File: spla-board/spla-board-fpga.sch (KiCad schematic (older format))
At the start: 4 parts, among them J2 J_JTAG, U1 LFE5U-45F-BG256

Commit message: schematic: Swap 0402 footprints for 0603.
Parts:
- R13, R14: footprint Resistor_SMD:R_0402_1005Metric -> Resistor_SMD:R_0603_1608Metric
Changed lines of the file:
@@
 F 0 "R13" H 3459 9796 50  0000 L CNN
 F 1 "4.7k" H 3459 9705 50  0000 L CNN
-F 2 "Resistor_SMD:R_0402_1005Metric" H 3400 9750 50  0001 C CNN
+F 2 "Resistor_SMD:R_0603_1608Metric" H 3400 9750 50  0001 C CNN
 F 3 "~" H 3400 9750 50  0001 C CNN
 	1    3400 9750
@@
 F 0 "R14" H 3459 10496 50  0000 L CNN
 F 1 "4.7k" H 3459 10405 50  0000 L CNN
-F 2 "Resistor_SMD:R_0402_1005Metric" H 3400 10450 50  0001 C CNN
+F 2 "Resistor_SMD:R_0603_1608Metric" H 3400 10450 50  0001 C CNN
 F 3 "~" H 3400 10450 50  0001 C CNN
 	1    3400 10450

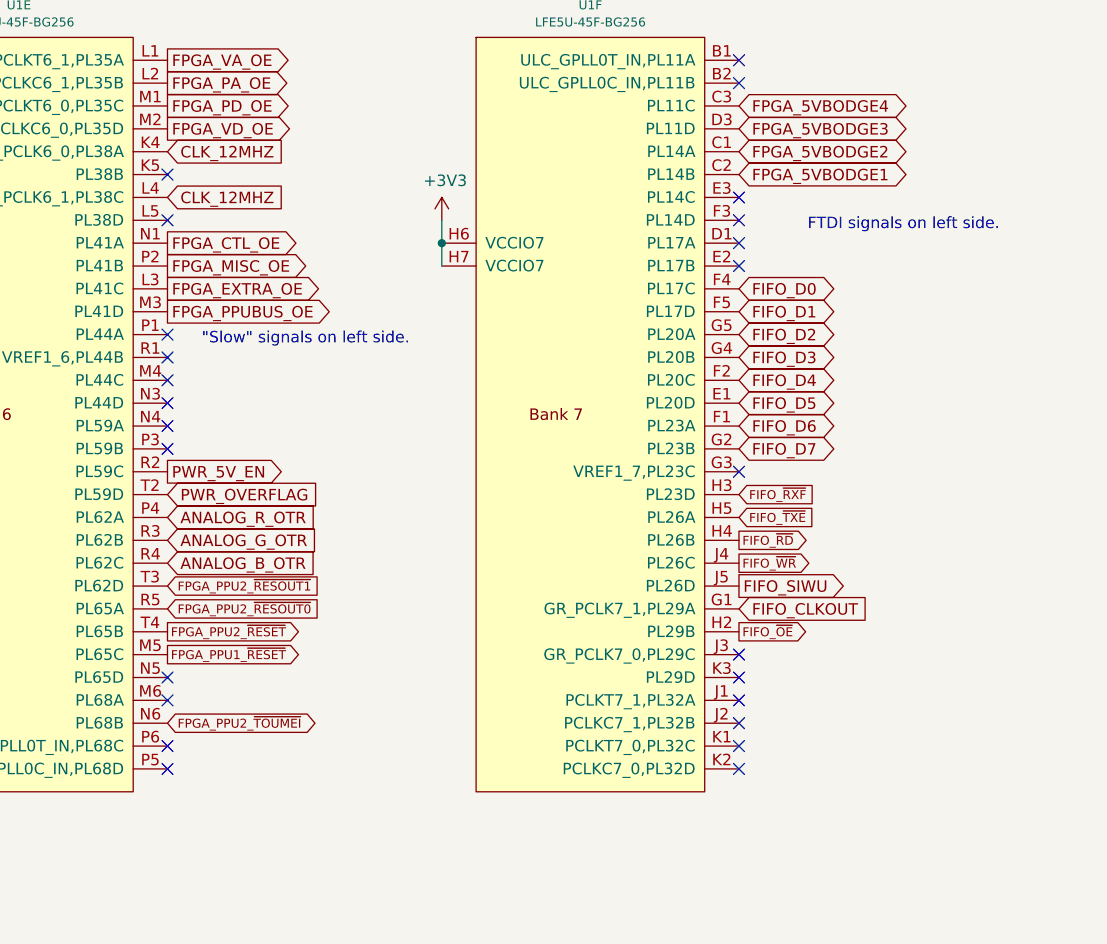
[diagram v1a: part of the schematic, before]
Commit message: schematic: Hook up TST pins to FPGA (via level shifters).
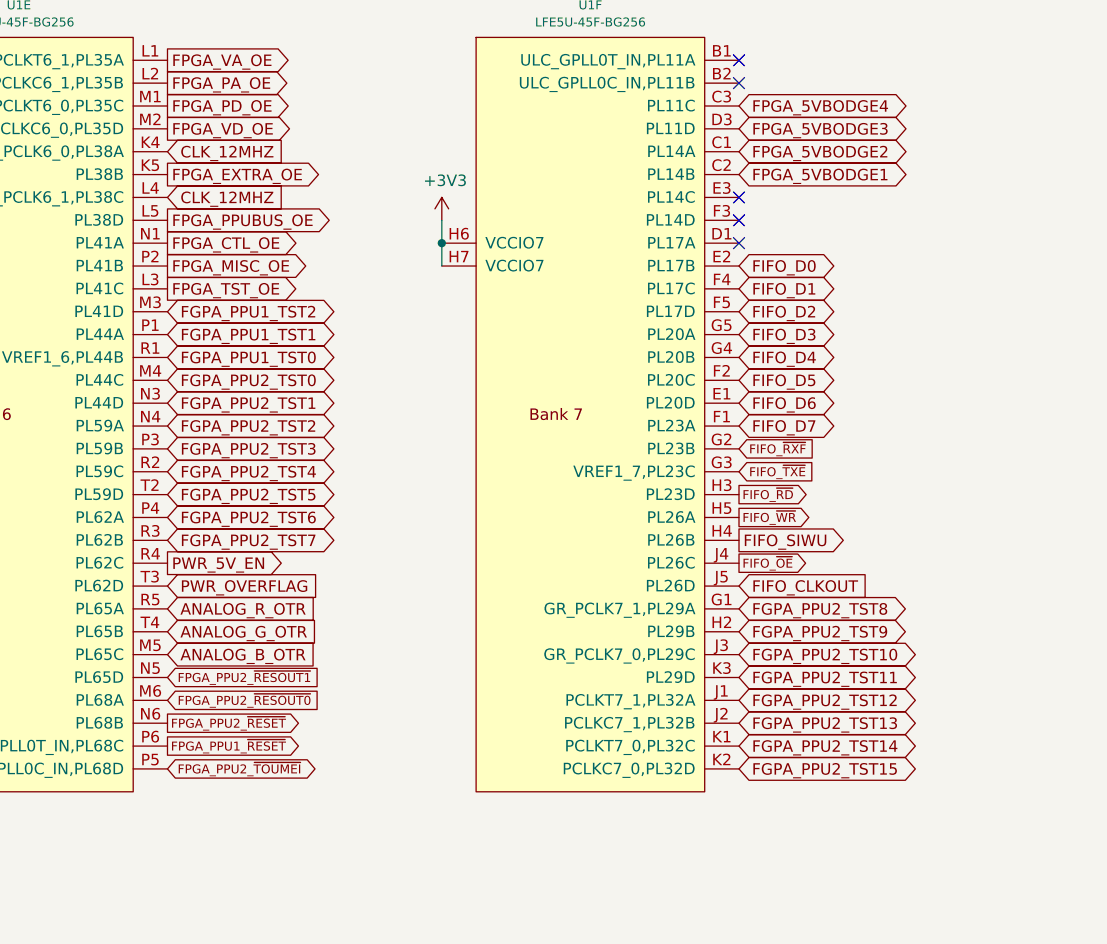
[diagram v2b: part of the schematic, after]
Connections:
- net ANALOG_B_OTR: now also U1.M5 (PL65C); no longer U1.R4 (PL62C)
- net ANALOG_G_OTR: now also U1.T4 (PL65B); no longer U1.R3 (PL62B)
- net ANALOG_R_OTR: now also U1.R5 (PL65A); no longer U1.P4 (PL62A)
- net FIFO_CLKOUT: now also U1.J5 (PL26D); no longer U1.G1 (GR_PCLK7_1,PL29A)
- net FIFO_D0: now also U1.E2 (PL17B); no longer U1.F4 (PL17C)
- net FIFO_D1: now also U1.F4 (PL17C); no longer U1.F5 (PL17D)
- net FIFO_D2: now also U1.F5 (PL17D); no longer U1.G5 (PL20A)
- net FIFO_D3: now also U1.G5 (PL20A); no longer U1.G4 (PL20B)
- net FIFO_D4: now also U1.G4 (PL20B); no longer U1.F2 (PL20C)
- net FIFO_D5: now also U1.F2 (PL20C); no longer U1.E1 (PL20D)
- net FIFO_D6: now also U1.E1 (PL20D); no longer U1.F1 (PL23A)
- net FIFO_D7: now also U1.F1 (PL23A); no longer U1.G2 (PL23B)
- net FIFO_SIWU: now also U1.H4 (PL26B); no longer U1.J5 (PL26D)
- net FIFO_~OE~: now also U1.J4 (PL26C); no longer U1.H2 (PL29B)
- net FIFO_~RD~: now also U1.H3 (PL23D); no longer U1.H4 (PL26B)
- net FIFO_~RXF~: now also U1.G2 (PL23B); no longer U1.H3 (PL23D)
- net FIFO_~TXE~: now also U1.G3 (VREF1_7,PL23C); no longer U1.H5 (PL26A)
- net FIFO_~WR~: now also U1.H5 (PL26A); no longer U1.J4 (PL26C)
- net FPGA_EXTRA_OE: now also U1.K5 (PL38B); no longer U1.L3 (PL41C)
- net FPGA_PPU1_~RESET~: now also U1.P6 (LLC_GPLL0T_IN,PL68C); no longer U1.M5 (PL65C)
- net FPGA_PPU2_~RESET~: now also U1.N6 (PL68B); no longer U1.T4 (PL65B)
- net FPGA_PPU2_~RESOUT0~: now also U1.M6 (PL68A); no longer U1.R5 (PL65A)
- net FPGA_PPU2_~RESOUT1~: now also U1.N5 (PL65D); no longer U1.T3 (PL62D)
- net FPGA_PPU2_~TOUMEI~: now also U1.P5 (LLC_GPLL0C_IN,PL68D); no longer U1.N6 (PL68B)
- net FPGA_PPUBUS_OE: now also U1.L5 (PL38D); no longer U1.M3 (PL41D)
- net PWR_5V_EN: now also U1.R4 (PL62C); no longer U1.R2 (PL59C)
- net PWR_OVERFLAG: now also U1.T3 (PL62D); no longer U1.T2 (PL59D)
- net FGPA_PPU2_TST0: now reaches U1.M4 (PL44C)
- net FGPA_PPU2_TST1: now reaches U1.N3 (PL44D)
- net FGPA_PPU2_TST2: now reaches U1.N4 (PL59A)
- net FGPA_PPU1_TST1: now reaches U1.P1 (PL44A)
- net FGPA_PPU2_TST3: now reaches U1.P3 (PL59B)
- net FGPA_PPU1_TST0: now reaches U1.R1 (VREF1_6,PL44B)
- net FGPA_PPU2_TST12: now reaches U1.J1 (PCLKT7_1,PL32A)
- net FGPA_PPU2_TST13: now reaches U1.J2 (PCLKC7_1,PL32B)
- net FGPA_PPU2_TST10: now reaches U1.J3 (GR_PCLK7_0,PL29C)
- net FGPA_PPU2_TST14: now reaches U1.K1 (PCLKT7_0,PL32C)
- net FGPA_PPU2_TST15: now reaches U1.K2 (PCLKC7_0,PL32D)
- net FGPA_PPU2_TST11: now reaches U1.K3 (PL29D)
- new net FGPA_PPU1_TST2: U1.M3 (PL41D)
- new net FGPA_PPU2_TST4: U1.R2 (PL59C)
- new net FGPA_PPU2_TST5: U1.T2 (PL59D)
- new net FGPA_PPU2_TST6: U1.P4 (PL62A)
- new net FGPA_PPU2_TST7: U1.R3 (PL62B)
- new net FGPA_PPU2_TST8: U1.G1 (GR_PCLK7_1,PL29A)
- new net FGPA_PPU2_TST9: U1.H2 (PL29B)
- new net FPGA_TST_OE: U1.L3 (PL41C)
- no-connect marks 35 -> 15
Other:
- note removed: ""Slow" signals on left side."
- note removed: "FTDI signals on left side."
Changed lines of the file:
@@
-$Comp
-L SPLA:LFE5U-45F-BG256 U1
-U 6 1 5FE8A82C
-P 14000 2850
-F 0 "U1" H 14000 4641 39  0000 C CNN
-F 1 "LFE5U-45F-BG256" H 14000 4566 39  0000 C CNN
-F 2 "Package_BGA:BGA-256_14.0x14.0mm_Layout16x16_P0.8mm_Ball0.45mm_Pad0.32mm_NSMD" H 13050 4850 39  0001 C CNN
-F 3 "" H 13050 4850 39  0001 C CNN
-	6    14000 2850
-	1    0    0    -1
-$EndComp
 $Comp
 L SPLA:LFE5U-45F-BG256 U1
@@
 	1    0    0    -1
 $EndComp
-Wire Wire Line
-	13350 2000 13350 2100
-Connection ~ 13350 2100
-Wire Wire Line
-	13350 2100 13350 2200
 Wire Wire Line
 	1800 7050 1800 7150
@@
 Text GLabel 7150 2300 2    50   Input ~ 0
 FPGA_PRIO0
-Text GLabel 12150 2400 2    50   Output ~ 0
+Text GLabel 12150 2000 2    50   Output ~ 0
 FPGA_PPUBUS_OE
 Text GLabel 4650 4300 2    39   Output ~ 0
@@
 Text GLabel 7150 1400 2    50   Input ~ 0
 FPGA_PPU2_VBLANK
-Text GLabel 12150 3800 2    39   Output ~ 0
+Text GLabel 12150 4200 2    39   Output ~ 0
 FPGA_PPU2_~RESET~
-Text GLabel 12150 3900 2    39   Output ~ 0
+Text GLabel 12150 4300 2    39   Output ~ 0
 FPGA_PPU1_~RESET~
-Text GLabel 12150 3700 2    39   Input ~ 0
+Text GLabel 12150 4100 2    39   Input ~ 0
 FPGA_PPU2_~RESOUT0~
-Text GLabel 12150 3600 2    39   Input ~ 0
+Text GLabel 12150 4000 2    39   Input ~ 0
 FPGA_PPU2_~RESOUT1~
-Text GLabel 12150 2300 2    50   Output ~ 0
+Text GLabel 12150 1800 2    50   Output ~ 0
 FPGA_EXTRA_OE
 Text GLabel 4650 3900 2    39   BiDi ~ 0
@@
 Text GLabel 4650 3100 2    50   Input ~ 0
 FPGA_PPU2_3.58M
-Text GLabel 12150 4200 2    39   BiDi ~ 0
+Text GLabel 12150 4400 2    39   BiDi ~ 0
 FPGA_PPU2_~TOUMEI~
 Text GLabel 7150 1300 2    50   Output ~ 0
@@
 Text GLabel 3100 7700 2    39   Input ~ 0
 SPI_~CS~
-Text GLabel 14650 3200 2    39   Input ~ 0
+Text GLabel 14650 3000 2    39   Input ~ 0
 FIFO_~RXF~
-Text GLabel 14650 3300 2    39   Input ~ 0
+Text GLabel 14650 3100 2    39   Input ~ 0
 FIFO_~TXE~
-Text GLabel 14650 3400 2    39   Output ~ 0
+Text GLabel 14650 3200 2    39   Output ~ 0
 FIFO_~RD~
+Text GLabel 14650 3300 2    39   Output ~ 0
+FIFO_~WR~
+Text GLabel 14650 3600 2    50   Input ~ 0
+FIFO_CLKOUT
 Text GLabel 14650 3500 2    39   Output ~ 0
-FIFO_~WR~
-Text GLabel 14650 3700 2    50   Input ~ 0
-FIFO_CLKOUT
-Text GLabel 14650 3800 2    39   Output ~ 0
 FIFO_~OE~
-Text GLabel 14650 3600 2    50   Output ~ 0
+Text GLabel 14650 3400 2    50   Output ~ 0
 FIFO_SIWU
-Text GLabel 14650 3000 2    50   BiDi ~ 0
+Text GLabel 14650 2900 2    50   BiDi ~ 0
 FIFO_D7
-Text GLabel 14650 2900 2    50   BiDi ~ 0
+Text GLabel 14650 2800 2    50   BiDi ~ 0
 FIFO_D6
-Text GLabel 14650 2800 2    50   BiDi ~ 0
+Text GLabel 14650 2700 2    50   BiDi ~ 0
 FIFO_D5
-Text GLabel 14650 2700 2    50   BiDi ~ 0
+Text GLabel 14650 2600 2    50   BiDi ~ 0
 FIFO_D4
-Text GLabel 14650 2600 2    50   BiDi ~ 0
+Text GLabel 14650 2500 2    50   BiDi ~ 0
 FIFO_D3
-Text GLabel 14650 2500 2    50   BiDi ~ 0
+Text GLabel 14650 2400 2    50   BiDi ~ 0
 FIFO_D2
-Text GLabel 14650 2400 2    50   BiDi ~ 0
+Text GLabel 14650 2300 2    50   BiDi ~ 0
 FIFO_D1
-Text GLabel 14650 2300 2    50   BiDi ~ 0
+Text GLabel 14650 2200 2    50   BiDi ~ 0
 FIFO_D0
 Text Notes 3900 7100 0    50   ~ 0
@@
 NoConn ~ 3100 8600
 NoConn ~ 3100 8700
-NoConn ~ 12150 4000
-NoConn ~ 12150 4100
-NoConn ~ 14650 3900
-NoConn ~ 14650 4000
-NoConn ~ 14650 4100
-NoConn ~ 14650 4200
-NoConn ~ 14650 4300
-NoConn ~ 14650 4400
-Text Notes 14950 2050 0    50   ~ 0
-FTDI signals on left side.
-Text Notes 12300 2550 0    50   ~ 0
-"Slow" signals on left side.
-NoConn ~ 12150 3000
-NoConn ~ 12150 2900
-NoConn ~ 12150 2800
-NoConn ~ 12150 2700
-NoConn ~ 12150 2600
-NoConn ~ 12150 2500
 NoConn ~ 14650 1300
 NoConn ~ 14650 1400
-NoConn ~ 14650 1900
-NoConn ~ 14650 2000
-NoConn ~ 14650 2100
-NoConn ~ 14650 2200
 Text Notes 8300 9000 0    50   ~ 0
 TODO: Add decoupling capacitors
@@
 	2250 9950 2900 9950
 NoConn ~ 3100 7900
-NoConn ~ 14650 3100
 Text GLabel 2150 2100 2    50   Input ~ 0
 ANALOG_R0
@@
 	850  2500 850  2600
 Connection ~ 850  2500
-Text GLabel 12150 3100 2    50   Output ~ 0
+Text GLabel 12150 3500 2    50   Output ~ 0
 PWR_5V_EN
-Text GLabel 12150 3200 2    50   Input ~ 0
+Text GLabel 12150 3600 2    50   Input ~ 0
 PWR_OVERFLAG
 $Comp
@@
 Text GLabel 12150 1700 2    50   Input ~ 0
 CLK_12MHZ
-NoConn ~ 12150 1800
-NoConn ~ 12150 2000
-NoConn ~ 12150 4300
-NoConn ~ 12150 4400
-Text GLabel 12150 3500 2    50   Input ~ 0
+Text GLabel 12150 3900 2    50   Input ~ 0
 ANALOG_B_OTR
-Text GLabel 12150 3400 2    50   Input ~ 0
+Text GLabel 12150 3800 2    50   Input ~ 0
 ANALOG_G_OTR
-Text GLabel 12150 3300 2    50   Input ~ 0
+Text GLabel 12150 3700 2    50   Input ~ 0
 ANALOG_R_OTR
+Wire Wire Line
+	13350 2100 13350 2200
+Wire Wire Line
+	13350 2000 13350 2100
+Connection ~ 13350 2100
+$Comp
+L SPLA:LFE5U-45F-BG256 U1
+U 6 1 5FE8A82C
+P 14000 2850
+F 0 "U1" H 14000 4641 39  0000 C CNN
+F 1 "LFE5U-45F-BG256" H 14000 4566 39  0000 C CNN
+F 2 "Package_BGA:BGA-256_14.0x14.0mm_Layout16x16_P0.8mm_Ball0.45mm_Pad0.32mm_NSMD" H 13050 4850 39  0001 C CNN
+F 3 "" H 13050 4850 39  0001 C CNN
+	6    14000 2850
+	1    0    0    -1
+$EndComp
+Text GLabel 12150 2600 2    50   BiDi ~ 0
+FGPA_PPU1_TST0
+Text GLabel 12150 2300 2    50   Output ~ 0
+FPGA_TST_OE
+Text GLabel 12150 2500 2    50   BiDi ~ 0
+FGPA_PPU1_TST1
+Text GLabel 12150 2400 2    50   BiDi ~ 0
+FGPA_PPU1_TST2
+Text GLabel 14650 4400 2    50   BiDi ~ 0
+FGPA_PPU2_TST15
+Text GLabel 14650 4300 2    50   BiDi ~ 0
+FGPA_PPU2_TST14
+Text GLabel 14650 4200 2    50   BiDi ~ 0
+FGPA_PPU2_TST13
+Text GLabel 14650 4100 2    50   BiDi ~ 0
+FGPA_PPU2_TST12
+Text GLabel 14650 4000 2    50   BiDi ~ 0
+FGPA_PPU2_TST11
+Text GLabel 14650 3900 2    50   BiDi ~ 0
+FGPA_PPU2_TST10
+Text GLabel 14650 3800 2    50   BiDi ~ 0
+FGPA_PPU2_TST9
+Text GLabel 14650 3700 2    50   BiDi ~ 0
+FGPA_PPU2_TST8
+Text GLabel 12150 3400 2    50   BiDi ~ 0
+FGPA_PPU2_TST7
+Text GLabel 12150 3300 2    50   BiDi ~ 0
+FGPA_PPU2_TST6
+Text GLabel 12150 3200 2    50   BiDi ~ 0
+FGPA_PPU2_TST5
+Text GLabel 12150 3100 2    50   BiDi ~ 0
+FGPA_PPU2_TST4
+Text GLabel 12150 3000 2    50   BiDi ~ 0
+FGPA_PPU2_TST3
+Text GLabel 12150 2900 2    50   BiDi ~ 0
+FGPA_PPU2_TST2
+Text GLabel 12150 2800 2    50   BiDi ~ 0
+FGPA_PPU2_TST1
+Text GLabel 12150 2700 2    50   BiDi ~ 0
+FGPA_PPU2_TST0
+NoConn ~ 14650 1900
+NoConn ~ 14650 2000
+NoConn ~ 14650 2100
 $EndSCHEMATC

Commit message: schematic: Hook up ~PWREN and ~SUSPEND.
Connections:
- net USB_~PWREN~: now reaches U1.E3 (PL14C)
- net USB_~SUSPEND~: now reaches U1.F3 (PL14D)
- no-connect marks 15 -> 13
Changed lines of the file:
@@
 Text GLabel 12150 2700 2    50   BiDi ~ 0
 FGPA_PPU2_TST0
-NoConn ~ 14650 1900
-NoConn ~ 14650 2000
 NoConn ~ 14650 2100
+Text GLabel 14650 1900 2    39   Input ~ 0
+USB_~PWREN~
+Text GLabel 14650 2000 2    39   Input ~ 0
+USB_~SUSPEND~
 $EndSCHEMATC

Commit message: schematic: Review TODOs and tweak a bit.
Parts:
- J2: symbol Connector:Conn_01x04_Male -> Connector_Generic:Conn_01x04
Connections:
- net JTAG_TCK: now also J2.3 (Pin_3); no longer J2.2 (Pin_2)
- net JTAG_TDI: now also J2.2 (Pin_2); no longer J2.3 (Pin_3)
- net JTAG_TDO: now also J2.1 (Pin_1); no longer J2.4 (Pin_4)
- net JTAG_TMS: now also J2.4 (Pin_4); no longer J2.1 (Pin_1)
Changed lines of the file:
@@
 $EndComp
 $Comp
-L Connector:Conn_01x04_Male J2
+L Connector_Generic:Conn_01x04 J2
 U 1 1 6001AFBA
-P 2800 9650
-F 0 "J2" V 2600 9650 50  0000 R CNN
-F 1 "J_JTAG" V 2700 9600 50  0000 C CNN
-F 2 "Connector_PinHeader_2.54mm:PinHeader_1x04_P2.54mm_Vertical" H 2800 9650 50  0001 C CNN
-F 3 "~" H 2800 9650 50  0001 C CNN
-	1    2800 9650
-	0    1    1    0
+P 2700 9650
+F 0 "J2" V 2800 9650 50  0000 R CNN
+F 1 "J_JTAG" V 2900 9600 50  0000 C CNN
+F 2 "Connector_PinHeader_2.54mm:PinHeader_1x04_P2.54mm_Vertical" H 2700 9650 50  0001 C CNN
+F 3 "~" H 2700 9650 50  0001 C CNN
+	1    2700 9650
+	0    -1   -1   0
 $EndComp
 Wire Wire Line
